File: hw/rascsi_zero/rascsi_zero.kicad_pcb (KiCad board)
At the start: 2 copper layers, 65 x 30 mm, 87 parts, among them IC1 SN74LS641-1DW, IC2 SN74LS641-1DW, IC3 SN74LS641-1DW, IC4 SN74LS641-1DW, J1 Raspberry_Pi_2_3, J2 DNP, J4 I2C Pinout, J6 CONNFLY DB-25, J7 DNP, X1 Mac, X2 Dogcow, X3 Mac, X4 Dogcow, X5 Dogcow, X6 Dogcow, X7 Pi

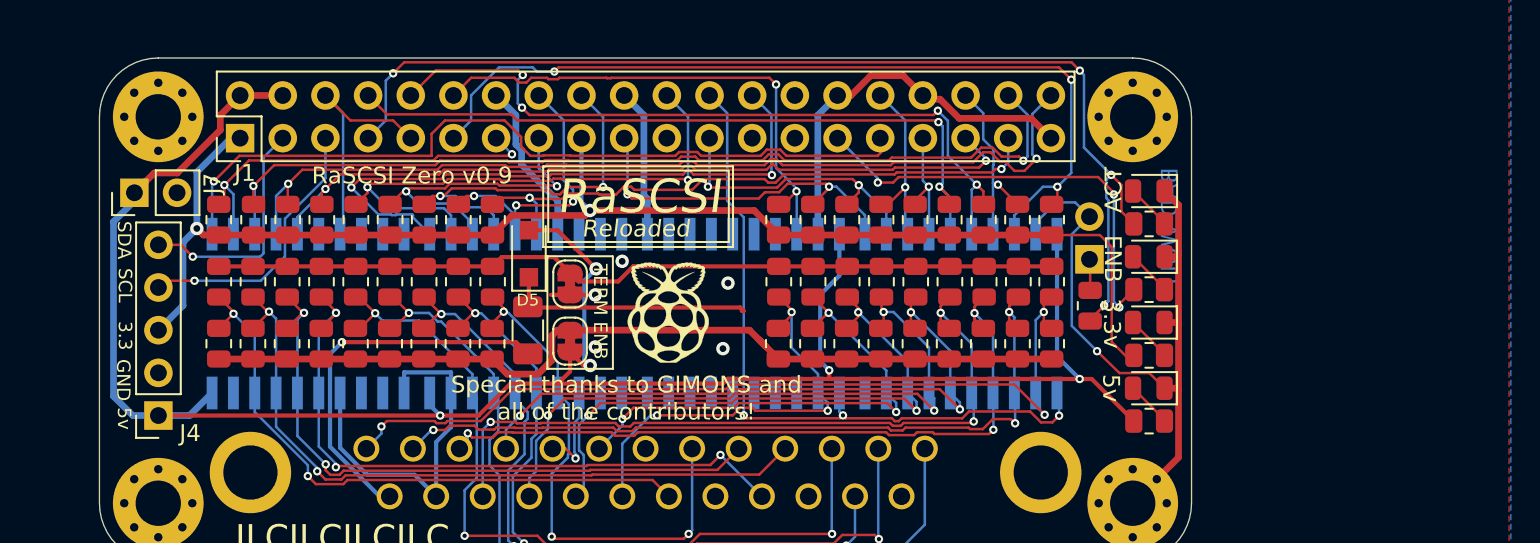
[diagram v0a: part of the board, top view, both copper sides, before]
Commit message: Add USB C Port
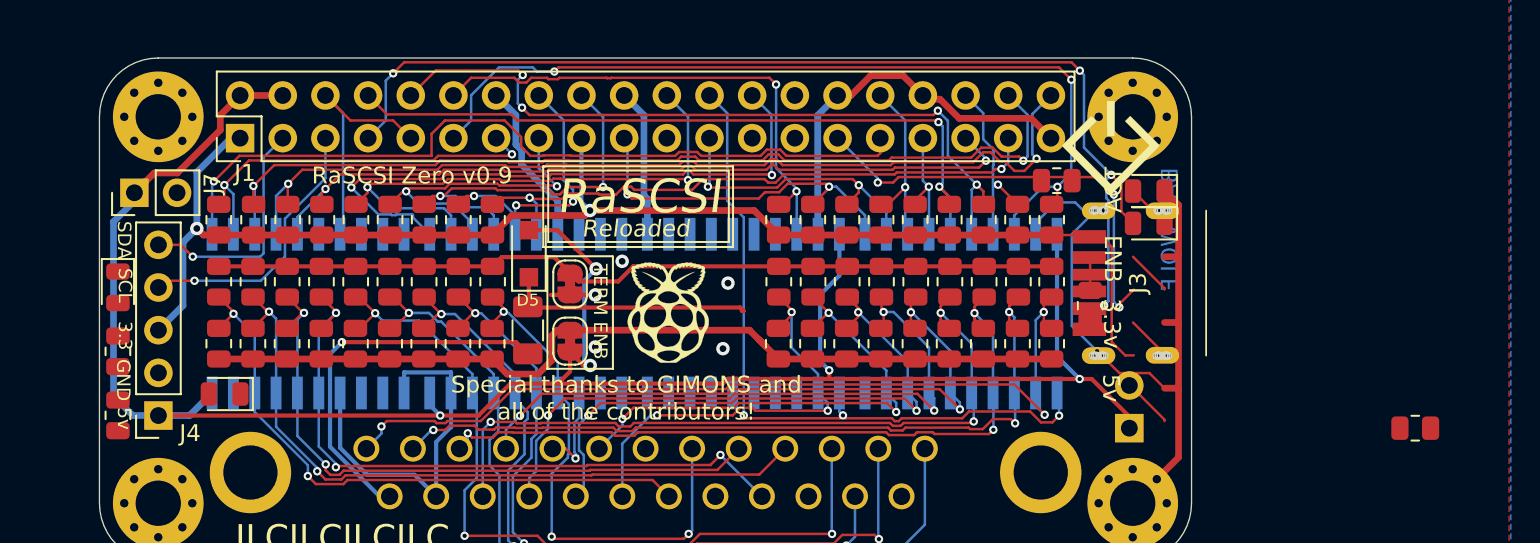
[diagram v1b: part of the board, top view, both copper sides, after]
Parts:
- added J3: TYPE-C-31-M-17, TYPE-C-31-M-17:TYPEC31M17, F.Cu at (240.4, 55.9)
- added X8: Pi, SamacSys_Parts:scsi_logo, F.Cu at (234.7, 47.8)
- moved D4 61.4 mm to (175.6, 56.1), turned to 270 degrees
- moved R3 61.4 mm to (175.6, 63.8), turned to 90 degrees
- moved R4 61.4 mm to (175.6, 60.0), turned to 90 degrees
- moved D3 55.0 mm to (181.9, 62.5)
- moved R2 17.9 mm to (252.8, 64.5)
- moved J2 10.3 mm to (235.8, 64.5)
- moved R1 6.07 mm to (231.5, 49.8)
- moved D2 1.99 mm to (237.0, 52.3)
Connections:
- J1 pad 21: (no net) -> Net-(J1-Pad21)
- J1 pad 27: (no net) -> Net-(J1-Pad27)
- J1 pad 28: (no net) -> Net-(J1-Pad28)
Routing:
- net Net-(D3-Pad2): track 2.73 -> 0.00 mm
- net GND: track 126.7 -> 129.5 mm

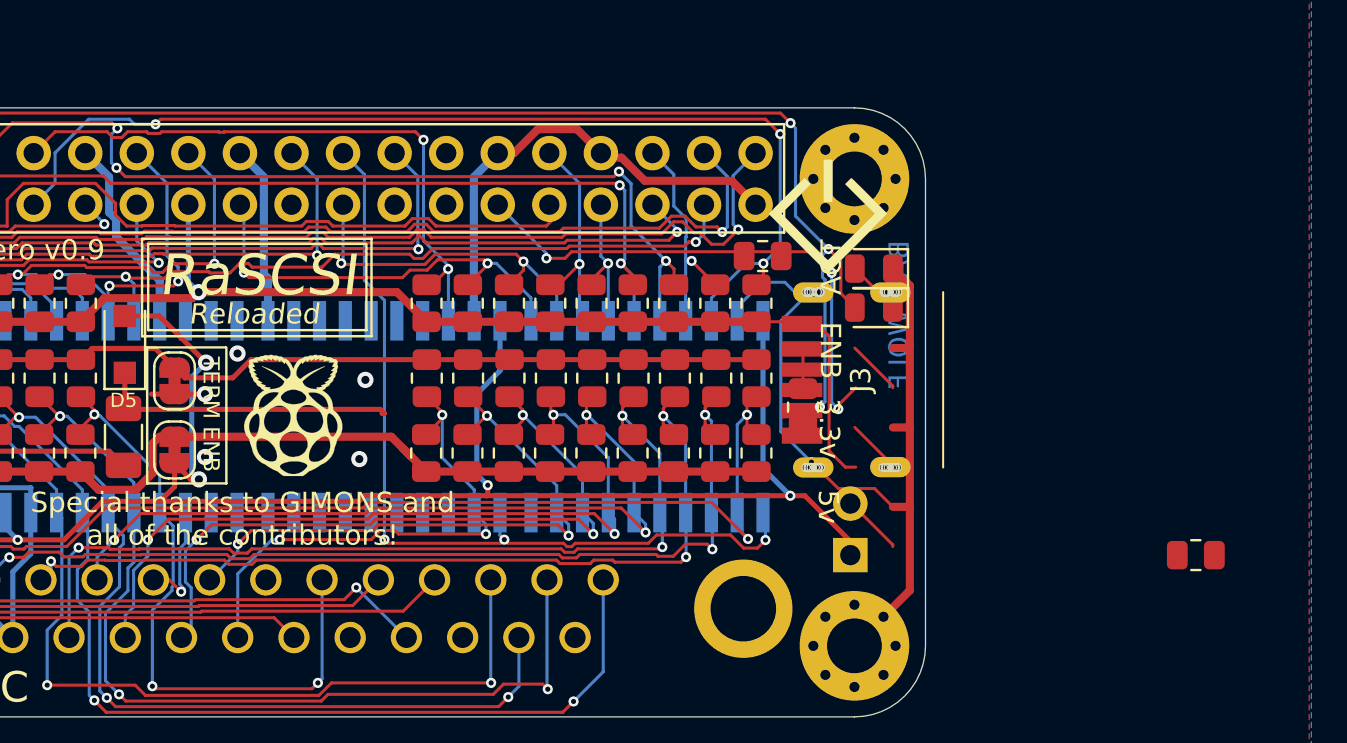
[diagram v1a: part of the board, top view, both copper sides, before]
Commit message: Updated with USBC port
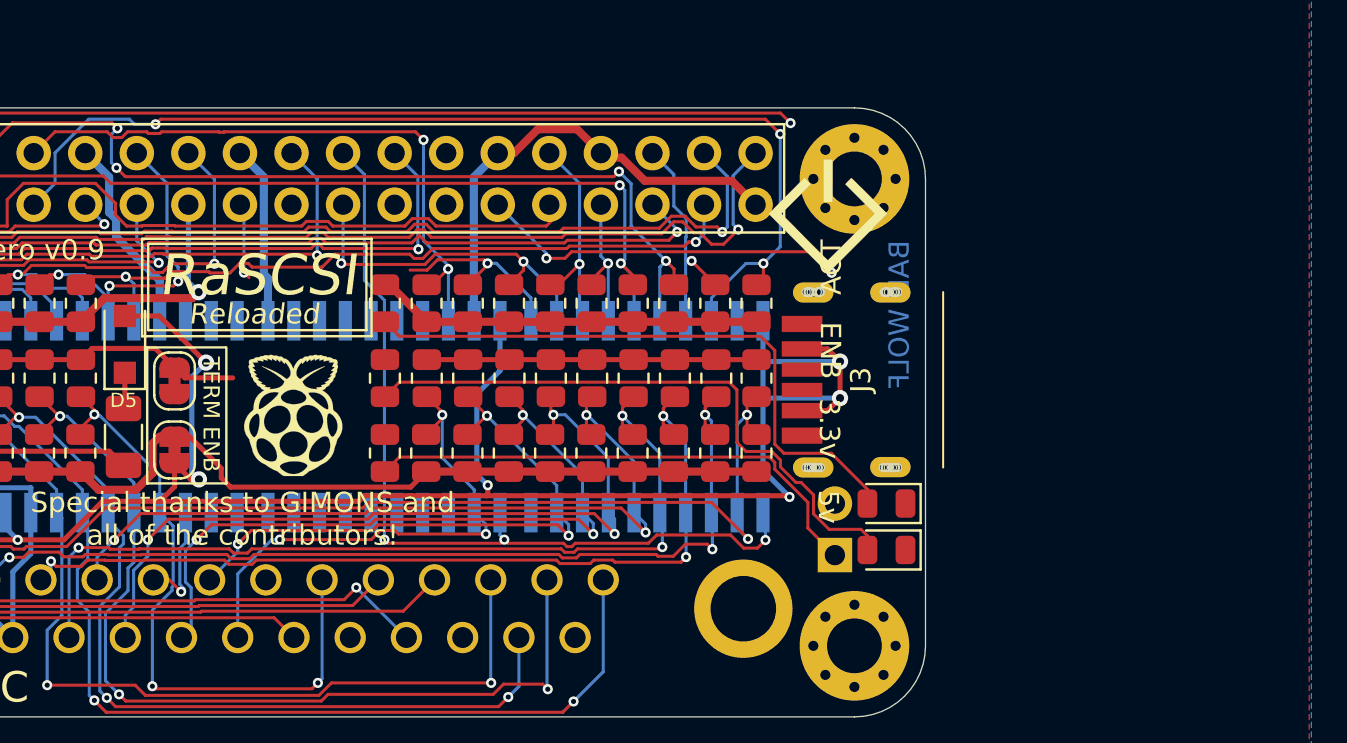
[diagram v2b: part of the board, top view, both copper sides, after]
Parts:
- moved R2 41.8 mm to (212.9, 52.1), turned to 270 degrees
- moved R59 20.7 mm to (212.9, 59.5), turned to 270 degrees
- moved R1 19.6 mm to (212.9, 55.8), turned to 270 degrees
- moved D1 13.9 mm to (237.6, 64.3)
- moved D2 9.67 mm to (237.6, 62.0)
- moved J2 0.76 mm to (235.0, 64.5)
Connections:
- J3 pad A12: Net-(J3-PadA12) -> GND
- J3 pad A9: Net-(J3-PadA9) -> +5V
- J3 pad B12: Net-(J3-PadB12) -> GND
- J3 pad B9: Net-(J3-PadB9) -> +5V
- J3 pad MH1: Net-(J3-PadMH1) -> GND
- J3 pad MH2: Net-(J3-PadMH2) -> GND
- J3 pad MH3: Net-(J3-PadMH3) -> GND
- J3 pad MH4: Net-(J3-PadMH4) -> GND
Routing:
- net GND: track 129.5 -> 85.4 mm, vias 7 -> 1
- net Net-(D2-Pad2): track 2.73 -> 30.6 mm
- net Net-(D1-Pad2): track 2.73 -> 30.2 mm
- net EXT-ACT-LED: track 1.87 -> 25.4 mm
- net +3V3: track 81.7 -> 60.8 mm
- net PI-ACT: track 65.6 -> 45.8 mm, vias 4 -> 2
- net Net-(D5-Pad1): track 14.9 -> 1.85 mm
- net /TERM_GND: track 51.9 -> 42.0 mm
- net +5V: track 126.3 -> 135.8 mm, vias 5 -> 7
- net DBG_LED: track 26.6 -> 18.3 mm, vias 3 -> 2
- net PI-D0: track 21.4 -> 13.3 mm
- net Net-(D4-Pad2): track 2.73 -> 0.00 mm

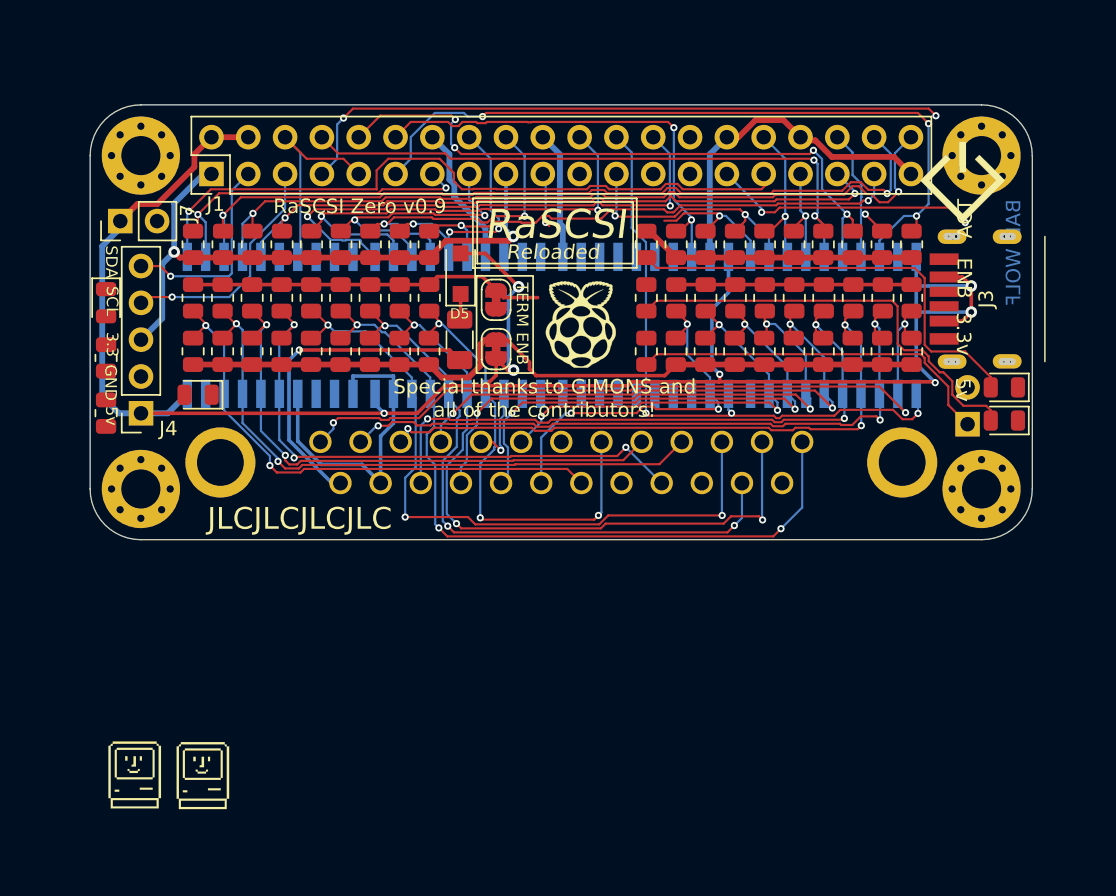
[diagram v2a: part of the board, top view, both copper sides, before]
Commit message: Routed and cleaned up USB C port
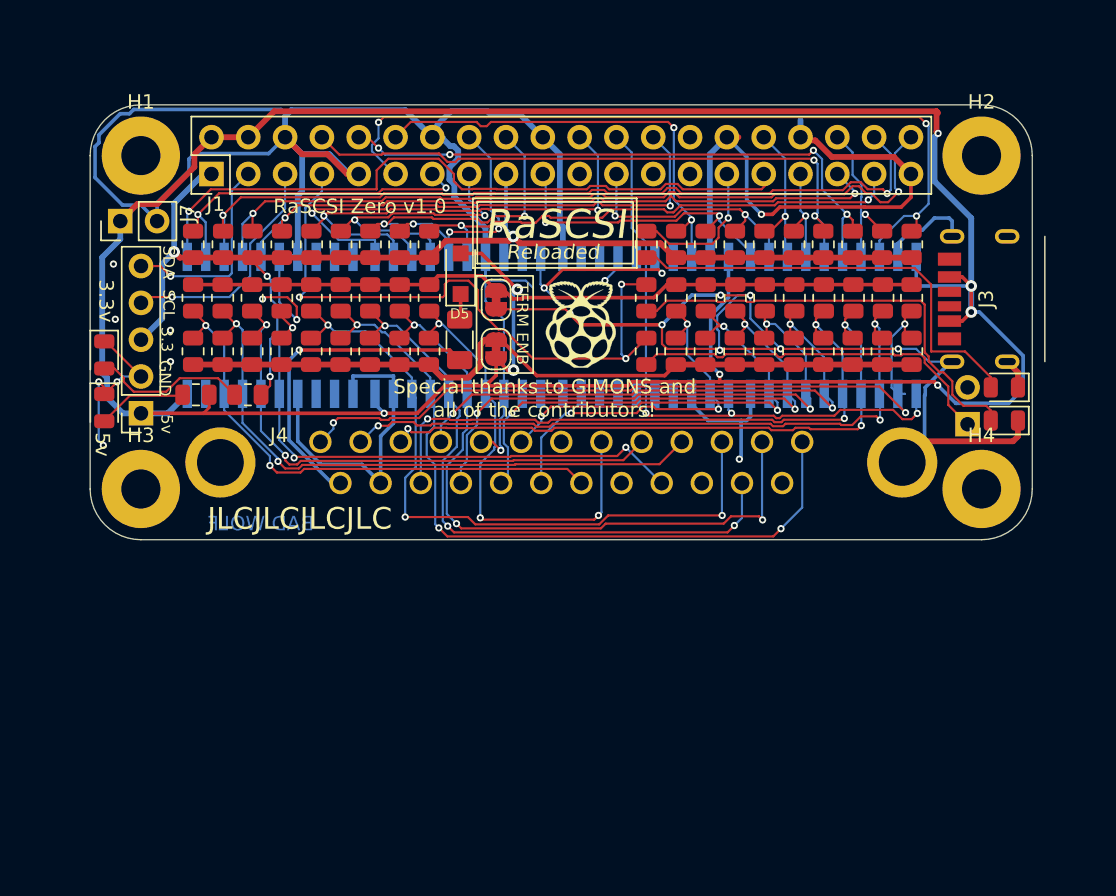
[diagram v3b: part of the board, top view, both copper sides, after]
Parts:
- removed X1, X3: Mac, SamacSys_Parts:mac_happy_small
- removed X8: Pi, SamacSys_Parts:scsi_logo
- H1, H2, H3, H4: footprint MountingHole:MountingHole_2.7mm_M2.5_Pad_Via -> MountingHole:MountingHole_2.7mm_M2.5_Pad
- moved R4 10.1 mm to (185.4, 62.5), turned to 180 degrees
- moved D3 6.54 mm to (175.5, 63.4), turned to 270 degrees
- moved R3 6.33 mm to (181.8, 62.5), turned to 180 degrees
- moved D4 3.61 mm to (175.5, 59.8)
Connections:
- H1 pad 1: GND -> (no net)
- H2 pad 1: GND -> (no net)
- H3 pad 1: GND -> (no net)
- H4 pad 1: GND -> (no net)
- J1 pad 21: Net-(J1-Pad21) -> (no net)
- J1 pad 27: Net-(J1-Pad27) -> (no net)
- J1 pad 28: Net-(J1-Pad28) -> (no net)
- J3 pad A5: Net-(J3-PadA5) -> (no net)
- J3 pad B5: Net-(J3-PadB5) -> (no net)
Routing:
- net GND: track 85.4 -> 305.7 mm, vias 1 -> 22
- net +5V: track 135.8 -> 203.1 mm, vias 7 -> 8
- net +3V3: track 60.8 -> 81.2 mm, vias 2 -> 4
- net Net-(D4-Pad2): track 0.00 -> 10.7 mm
- net /TERM_GND: track 42.0 -> 52.0 mm
- net DBG_LED: track 18.3 -> 10.2 mm, vias 2 -> 1
- net PI-D0: track 13.3 -> 20.9 mm
- net Net-(D3-Pad2): track 0.00 -> 6.17 mm
- net PI-D7: track 52.2 -> 54.9 mm
- net PI-D5: track 44.4 -> 41.8 mm
- net PI-ACT: track 45.8 -> 44.5 mm, vias 2 -> 3
- net C-D7: track 51.8 -> 52.7 mm
- net Net-(D1-Pad2): track 30.2 -> 30.7 mm
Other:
- board text added: "RaSCSI Zero v1.0"
- board text added: "RaSCSI Zero v1.0 FULLSPEC Version"
- board text removed: "RaSCSI Zero v0.9"
- board text removed: "RaSCSI Zero v0.9 FULLSPEC Version"

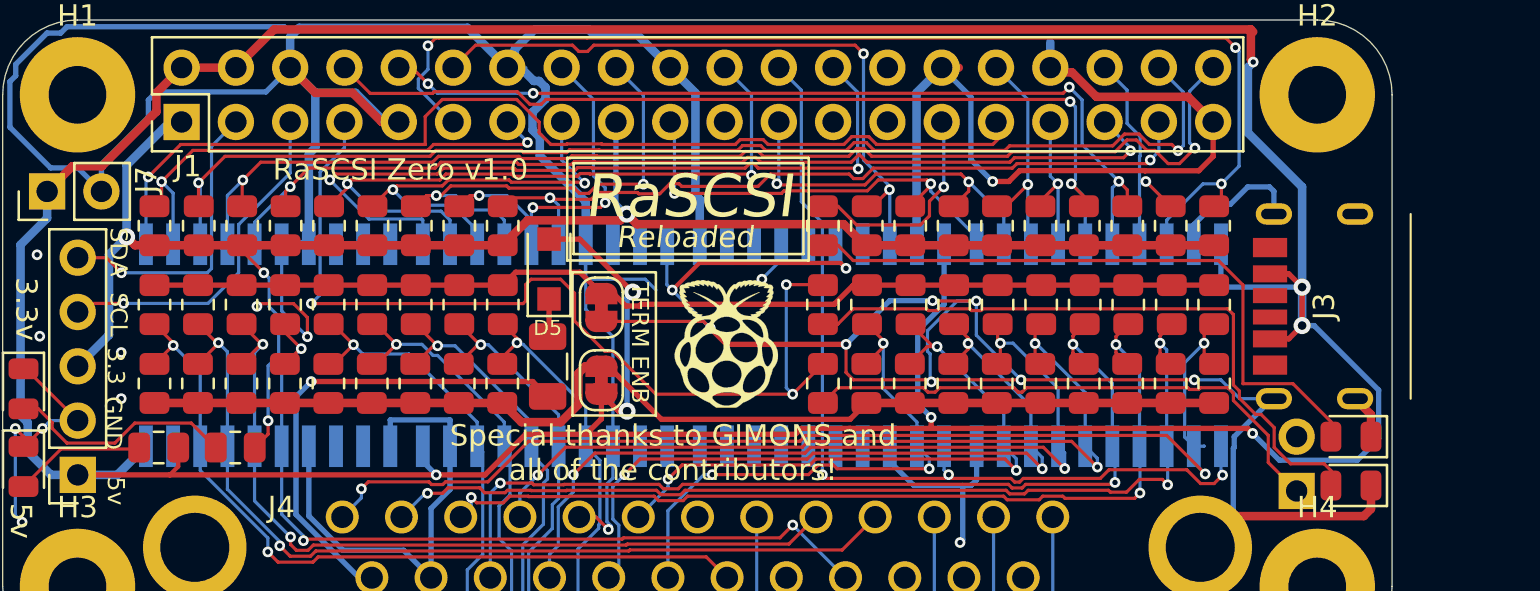
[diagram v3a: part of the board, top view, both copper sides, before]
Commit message: Changed USB port back to Micro. As-ordered 1p0
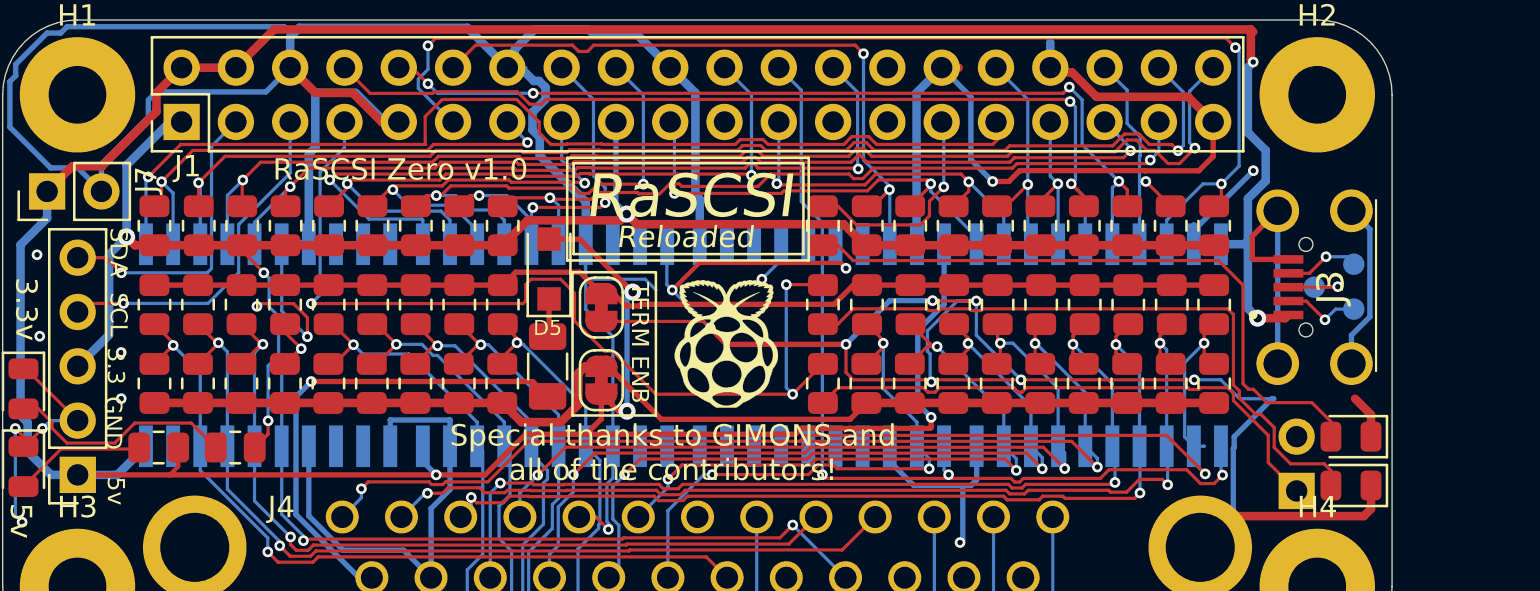
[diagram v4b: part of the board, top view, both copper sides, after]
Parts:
- added TP1: TestPoint_Small, TestPoint:TestPoint_Pad_D1.0mm, B.Cu at (237.7, 56.0)
- added TP2: TestPoint_Small, TestPoint:TestPoint_Pad_D1.0mm, B.Cu at (235.9, 55.0)
- added TP3: TestPoint_Small, TestPoint:TestPoint_Pad_D1.0mm, B.Cu at (237.7, 53.9)
- J3: value TYPE-C-31-M-17 -> U254-051N-4BH806; footprint TYPE-C-31-M-17:TYPEC31M17 -> SamacSys_Parts:U254051N4BH806
- moved J3 3.84 mm to (236.6, 55.0)
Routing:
- net +5V: track 203.1 -> 164.5 mm, vias 8 -> 6
- net GND: track 305.7 -> 324.6 mm, vias 22 -> 23
- net Net-(J3-Pad2): track 0.00 -> 3.63 mm, vias 0 -> 1
- net Net-(J3-Pad4): track 0.00 -> 3.53 mm, vias 0 -> 1
- net Net-(J3-Pad3): track 0.00 -> 3.43 mm, vias 0 -> 1
